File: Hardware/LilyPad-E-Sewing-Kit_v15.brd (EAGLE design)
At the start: 50.9 x 52.1 mm, 53 parts

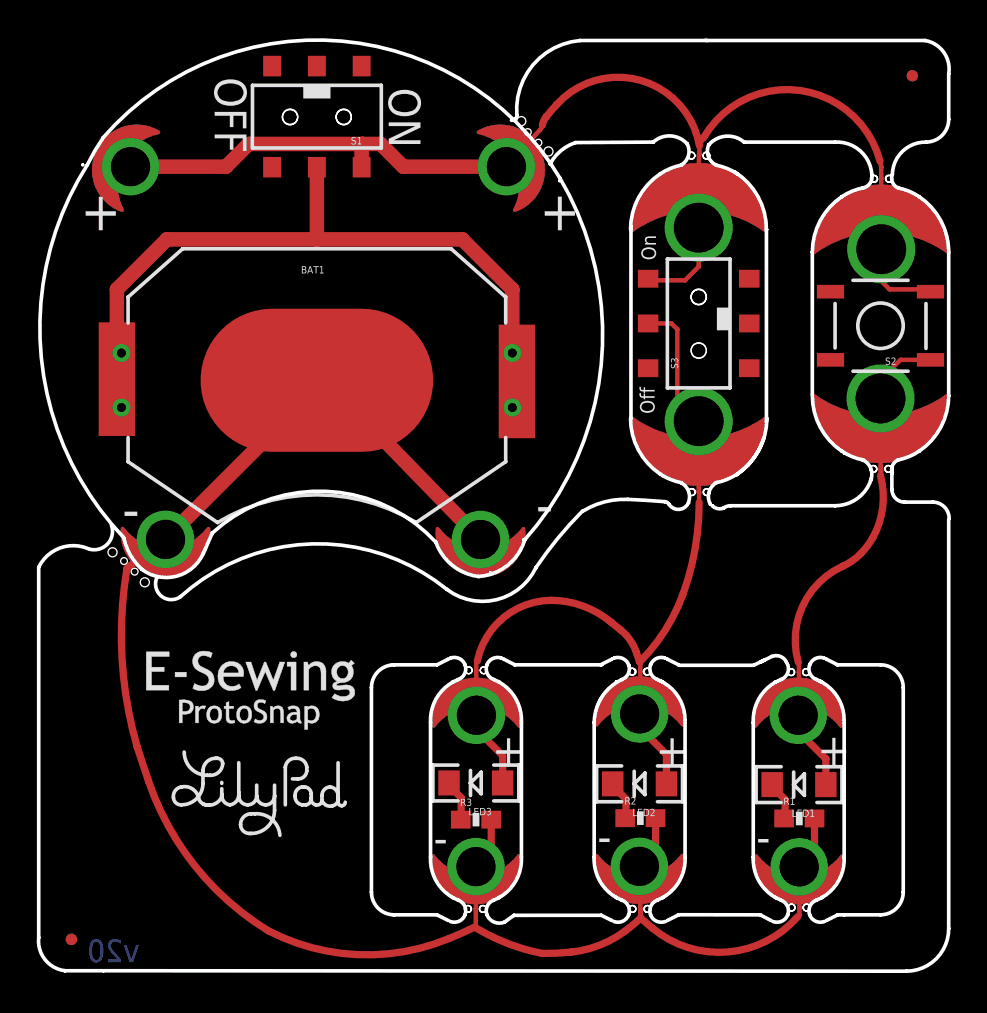
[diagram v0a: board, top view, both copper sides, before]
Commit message: Revert "Put it back on grid...."
This reverts commit 080445da69f31666997101091cdcd3686e199cd1.
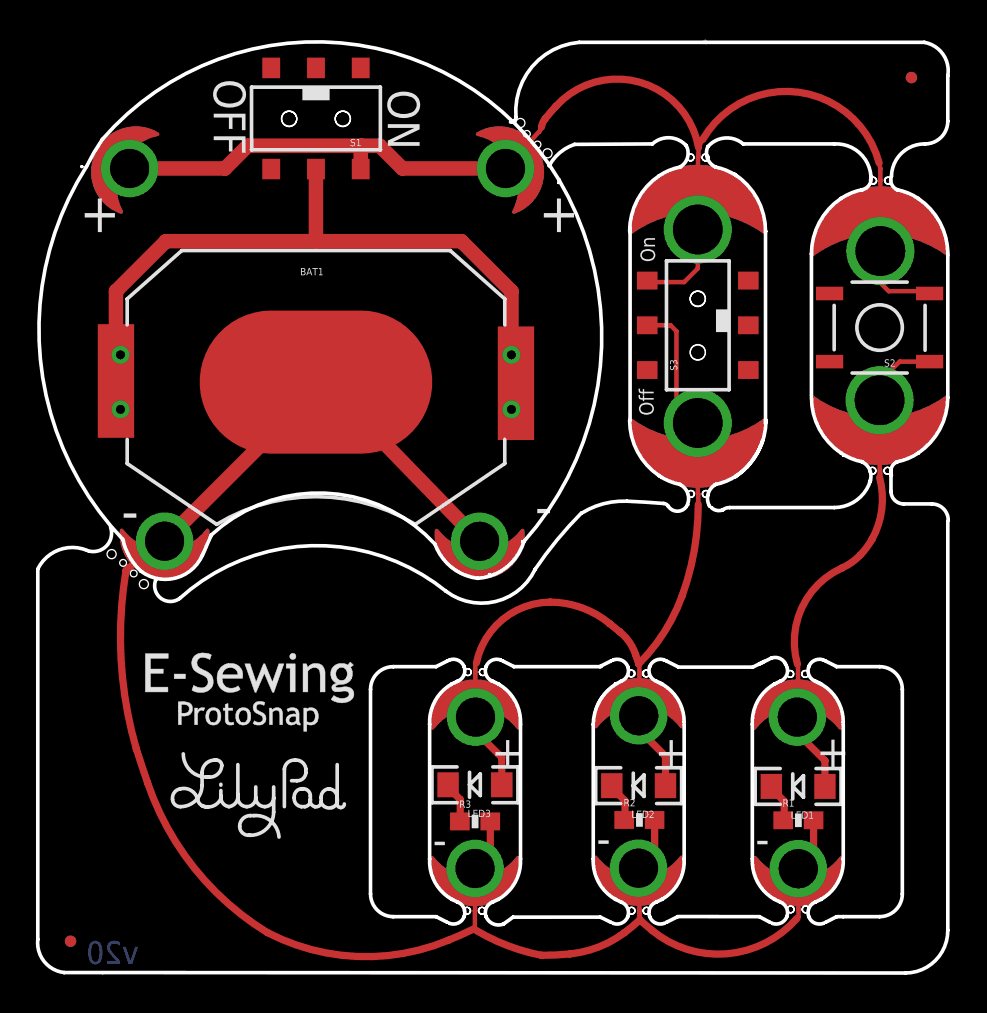
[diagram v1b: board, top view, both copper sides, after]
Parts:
- moved S3 0.11 mm to (36.8, 36.1)
- moved SLIDEON 0.11 mm to (36.8, 41.2)
- moved LED+2 0.11 mm to (33.5, 14.2)
- moved LED1 0.11 mm to (42.4, 10.3)
- moved LED2 0.11 mm to (33.5, 10.3)
- moved R2 0.11 mm to (33.6, 8.43)
- moved MB6 0.11 mm to (24.4, 3.35)
- moved MB8 0.11 mm to (42.4, 3.43)
- moved BATB- 0.11 mm to (7.04, 24.0)
- moved MB- 0.11 mm to (5.00, 22.5)
- moved LED-1 0.11 mm to (42.4, 5.70)
- moved LED3 0.11 mm to (24.4, 10.4)
- moved BATB-2 0.11 mm to (24.6, 24.0)
- moved LED+3 0.11 mm to (24.4, 14.2)
- moved MB5 0.11 mm to (24.4, 16.7)
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
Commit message: Picked a different grid....
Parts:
- moved BAT1 0.20 mm to (15.5, 33.1)
- moved BATB-2 0.20 mm to (24.6, 24.2)
- moved BUTTON- 0.20 mm to (47.0, 40.2)
- moved BUTTONS 0.20 mm to (47.0, 32.3)
- moved LOGO1 0.20 mm to (11.0, 46.6)
- moved MB2 0.20 mm to (47.0, 44.4)
- moved MB4 0.20 mm to (33.6, 16.8)
- moved S1 0.20 mm to (15.5, 47.8)
- moved S3 0.20 mm to (36.8, 36.3)
- moved SLIDEON 0.20 mm to (36.8, 41.4)
- moved U$3 0.20 mm to (15.3, 36.7)
- moved U$5 0.20 mm to (36.3, 35.7)
- moved U$6 0.20 mm to (46.0, 35.7)
- moved LED+1 0.20 mm to (42.4, 14.4)
- moved LED+2 0.20 mm to (33.5, 14.5)
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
